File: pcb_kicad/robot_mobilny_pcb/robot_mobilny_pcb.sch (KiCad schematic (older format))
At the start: 25 parts, among them J2 BOOT0, J3 TOP_CONN, J4 BOOT1, J5 RIGHT_CONN, J6 LEFT_CONN, J7 BOTTOM_CONN, SW2 RESET, U1 STM32F411RETx, Y1 8Mhz, Y2 Crystal

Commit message: schematic update
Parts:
- removed J3: TOP_CONN, symbol Connector:Conn_01x16_Female
- removed J5: RIGHT_CONN, symbol Connector:Conn_01x16_Female
- removed J6: LEFT_CONN, symbol Connector:Conn_01x16_Female
- removed J7: BOTTOM_CONN, symbol Connector:Conn_01x16_Female
- removed JP?: boot_1_mode, symbol Device:Jumper
- removed JP?: boot_mode, symbol Device:Jumper
- added JP? (x8): Jumper_3_Bridged12, Connector_PinHeader_2.54mm:PinHeader_1x03_P2.54mm_Vertical, symbol Jumper:Jumper_3_Bridged12
- J1: renamed from J2; footprint (none) -> Connector_PinSocket_2.54mm:PinSocket_1x03_P2.54mm_Vertical
- J3: renamed from J4; footprint (none) -> Connector_PinSocket_2.54mm:PinSocket_1x03_P2.54mm_Vertical
- SW1: renamed from SW2; footprint (none) -> Button_Switch_THT:SW_PUSH_6mm_H9.5mm
- gave numbers to parts that had none: 1
- renumbered C5 to C1, C6 to C2, C7 to C3, C8 to C4, C9 to C5, C10 to C6, R9 to R2, R10 to R3, R11 to R4, R12 to R5, R13 to R6, R14 to R7
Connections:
- net labels added: ADC_BAT, BOOT0, Dist_Sens_01_Echo, Dist_Sens_01_Trig, Dist_Sens_02_Echo, Dist_Sens_02_Trig, Dist_Sens_03_Echo, Dist_Sens_03_Trig, Dist_Sens_04_Echo, Dist_Sens_04_Trig, Dist_Sens_05_Echo, Dist_Sens_05_Trig, Dist_Sens_06_Echo, Dist_Sens_06_Trig, I2C2_SCL_mag+acc, I2C2_SDA_mag+acc, INT1_mag+acc, INT2_mag+acc, NRST, PD2
- net labels removed: LED5, SPI2_MISO, SPI2_MOSI
- wire segments 95 -> 112
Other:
- note removed: "pomiar prady z silnikow\n"
- moved on the sheet: C1, C2, C3, C4, C5, C6, J1, J3, R1, R2, R3, R4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

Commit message: schematic_update
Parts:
- C101: renamed from C1; value 0.1uF -> 100nF; footprint (none) -> Capacitor_THT:C_Disc_D5.0mm_W2.5mm_P2.50mm
- J101: renamed from J1; footprint Connector_PinSocket_2.54mm:PinSocket_1x03_P2.54mm_Vertical -> Connector_PinHeader_2.54mm:PinHeader_1x03_P2.54mm_Vertical
- J102: renamed from J3; footprint Connector_PinSocket_2.54mm:PinSocket_1x03_P2.54mm_Vertical -> Connector_PinHeader_2.54mm:PinHeader_1x03_P2.54mm_Vertical
- R101: renamed from R1; footprint (none) -> Resistor_THT:R_Axial_DIN0207_L6.3mm_D2.5mm_P10.16mm_Horizontal
- R102: renamed from R2; footprint (none) -> Resistor_THT:R_Axial_DIN0207_L6.3mm_D2.5mm_P10.16mm_Horizontal
- R105: renamed from R5; footprint (none) -> Resistor_THT:R_Axial_DIN0207_L6.3mm_D2.5mm_P10.16mm_Horizontal
- Y101: renamed from Y1; footprint (none) -> Crystal:Crystal_HC49-4H_Vertical
- Y102: renamed from Y2; footprint (none) -> Crystal:Crystal_HC49-4H_Vertical
- gave numbers to parts that had none: 8
- renumbered C2 to C102, C3 to C103, C4 to C104, C5 to C105, C6 to C106, R3 to R103, R4 to R104, R6 to R106, R7 to R107, SW1 to SW101, U1 to U101

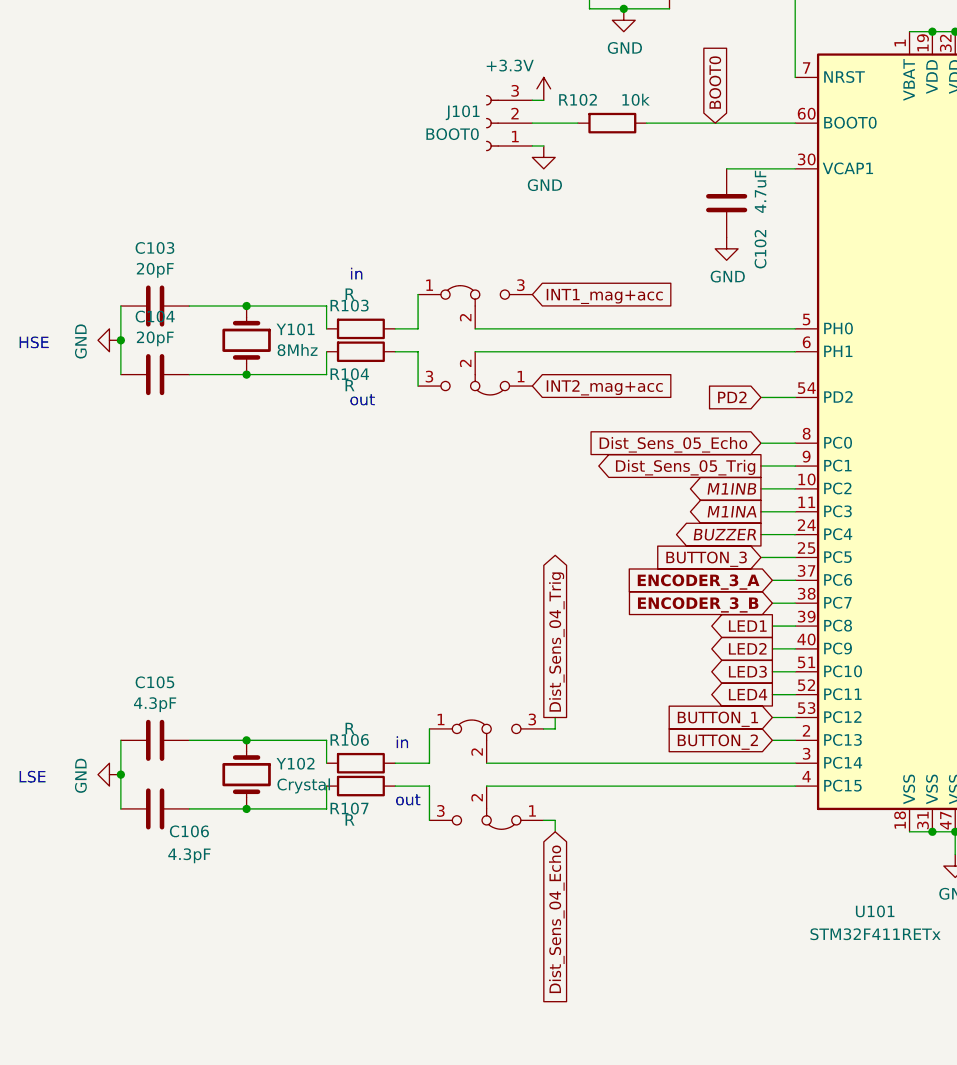
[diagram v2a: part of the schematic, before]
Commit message: PCB_update
Change of  motor controller connector to Arduino shields
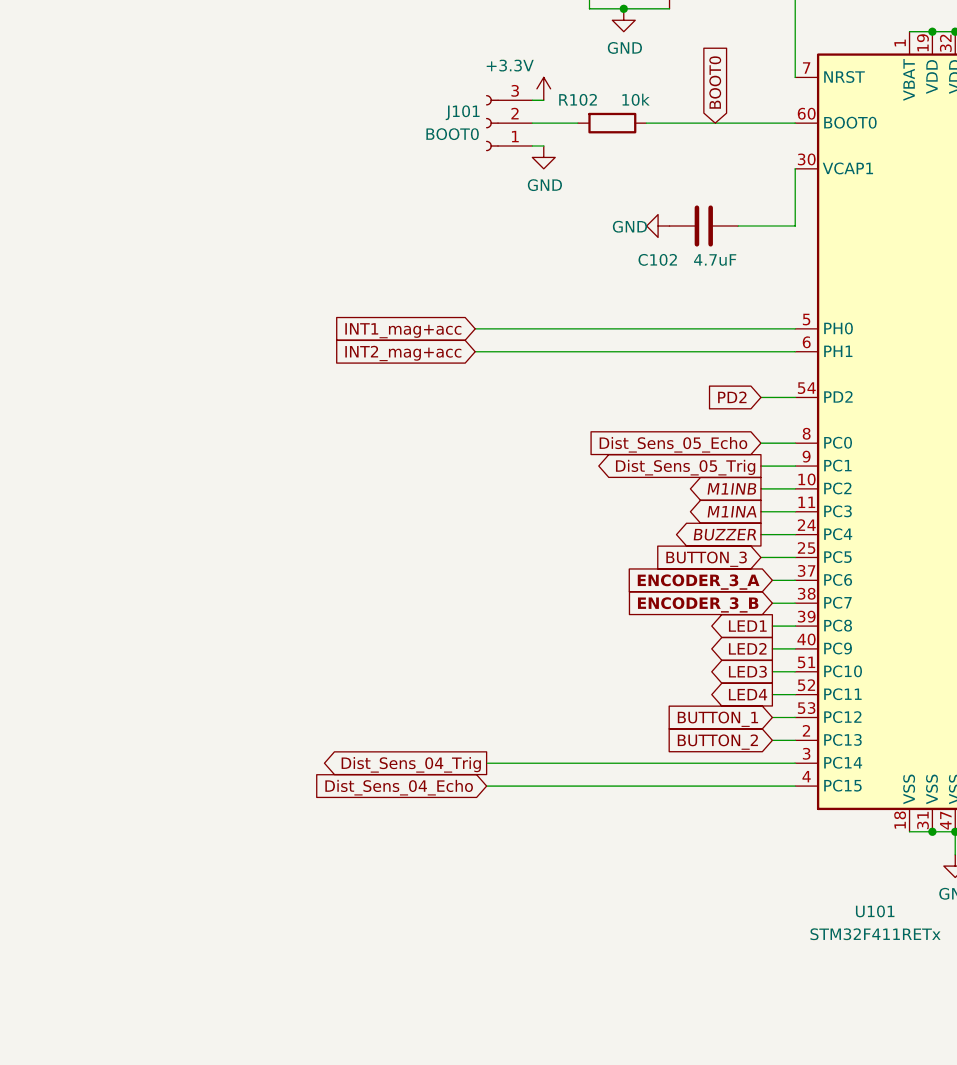
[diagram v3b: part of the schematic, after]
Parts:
- removed C103, C104: 20pF, symbol Device:C
- removed C105, C106: 4.3pF, symbol Device:C
- removed JP101, JP103, JP106, JP108: Jumper_3_Bridged12, Connector_PinHeader_2.54mm:PinHeader_1x03_P2.54mm_Vertical, symbol Jumper:Jumper_3_Bridged12
- removed R103, R104, R106, R107: R, symbol Device:R
- removed Y101: 8Mhz, Crystal:Crystal_HC49-4H_Vertical, symbol Device:Crystal
- removed Y102: Crystal, Crystal:Crystal_HC49-4H_Vertical, symbol Device:Crystal
- C102: footprint (none) -> Capacitor_THT:C_Disc_D5.0mm_W2.5mm_P2.50mm
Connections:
- net Dist_Sens_04_Echo: now also U101.4 (PC15)
- net Dist_Sens_04_Trig: now also U101.3 (PC14)
- net INT1_mag+acc: now also U101.5 (PH0)
- net INT2_mag+acc: now also U101.6 (PH1)
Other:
- note removed: "HSE"
- note removed: "LSE"
- note removed: "in"
- note removed: "out"
- moved on the sheet: C102

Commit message: PCB_update
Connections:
- net PB2: now reaches JP105.2 (C), U101.28 (PB2)
- net VCAP_1: now reaches C102.1, U101.30 (VCAP1)
- net PA11: now reaches JP102.2 (C), U101.44 (PA11)
- net PA12: now reaches JP104.2 (C), U101.45 (PA12)
- net PB9: now reaches JP107.2 (C), U101.61 (PB8)
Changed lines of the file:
@@
 	4500 5350 4600 5350
 Wire Wire Line
-	5300 3950 6150 3950
+	5300 3950 6100 3950
 $Comp
 L Jumper:Jumper_3_Bridged12 JP107
@@
 Wire Wire Line
 	3900 2700 3900 2450
+Text GLabel 3900 2450 0    50   Input ~ 0
+VCAP_1
+Text GLabel 6400 4600 2    50   Output ~ 10
+PB9
+Text GLabel 6250 3600 1    50   Output ~ 10
+PB2
+Wire Wire Line
+	6250 3600 6250 3900
+Wire Wire Line
+	6250 3900 6100 3900
+Wire Wire Line
+	6100 3900 6100 3950
+Connection ~ 6100 3950
+Wire Wire Line
+	6100 3950 6150 3950
+Text GLabel 6650 3150 1    50   Output ~ 10
+PA11
+Text GLabel 6650 3250 3    50   Output ~ 10
+PA12
 $EndSCHEMATC
